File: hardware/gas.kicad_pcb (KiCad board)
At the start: 2 copper layers, 50 x 30 mm, 41 parts, among them P1 CON-SENSOR2, P10 3, P2 DEBUG, P3 BOOT, P7 0, P8 1, P9 2, U1 XMC1300, U10 MCP3423, U11 spec-sensor, U2 DRILL, U3 DRILL, U4 DRILL, U5 DRILL, U6 HDC1080, U7 ISL60002, U8 LMP91000, U9 MCP6041

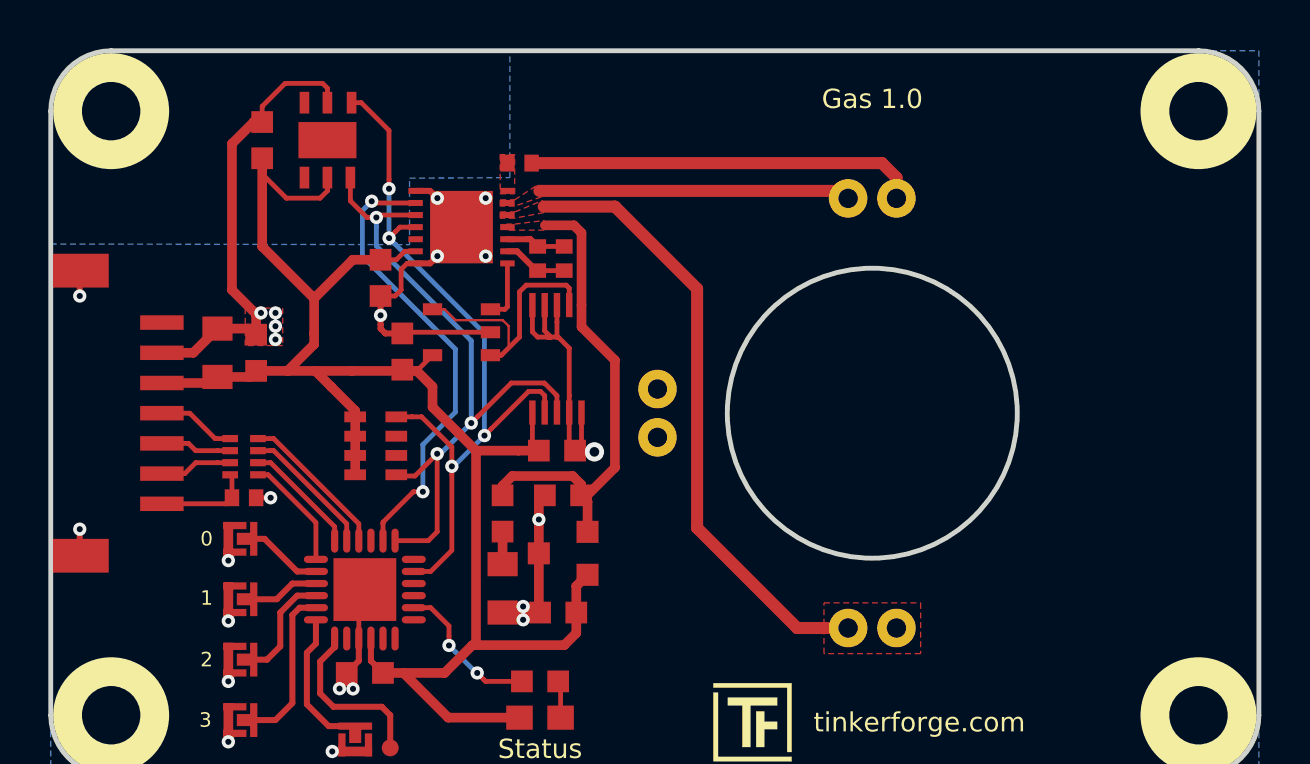
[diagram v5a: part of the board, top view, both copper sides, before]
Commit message: add fiducials
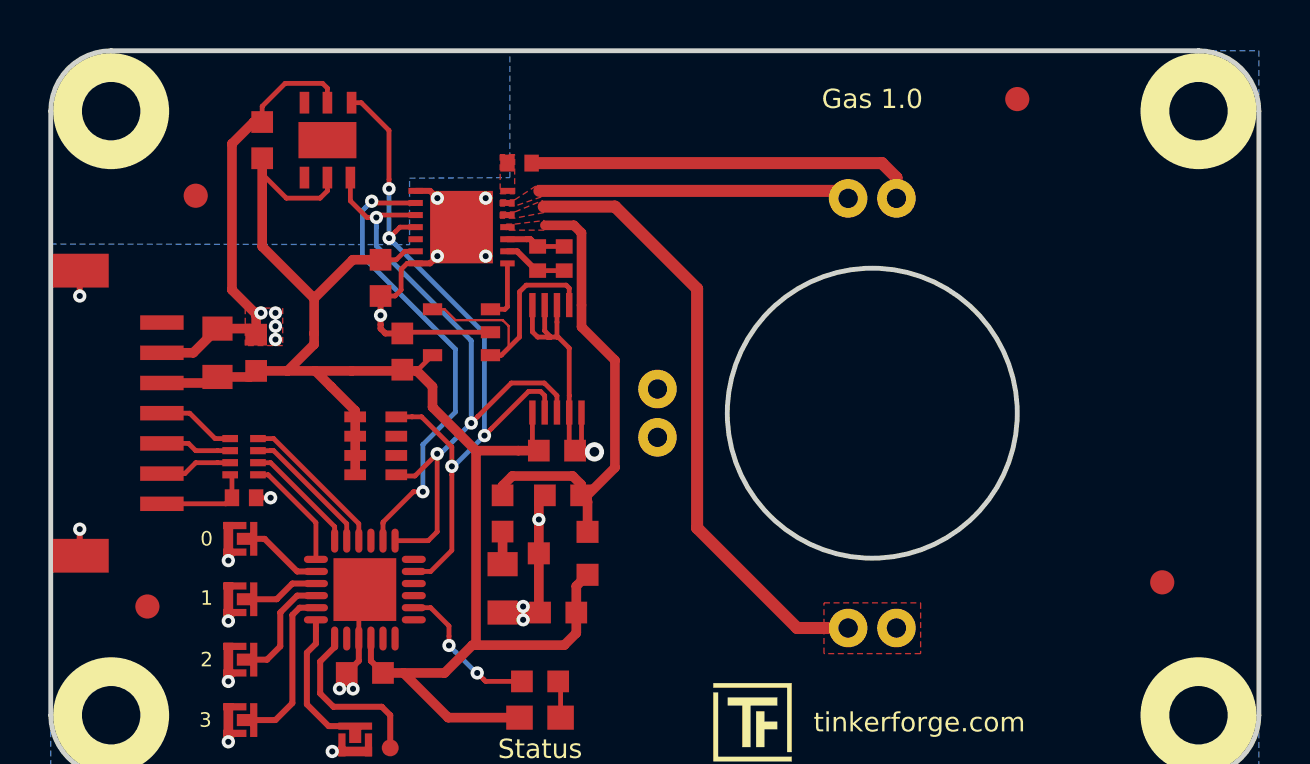
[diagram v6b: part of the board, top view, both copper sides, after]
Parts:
- added Fiducial_Mark: VAL**, kicad-libraries:Fiducial_Mark, F.Cu at (131.0, 122.1)
- added Fiducial_Mark: VAL**, kicad-libraries:Fiducial_Mark, F.Cu at (129.0, 139.1)
- added Fiducial_Mark: VAL**, kicad-libraries:Fiducial_Mark, F.Cu at (171.0, 138.1)
- added Fiducial_Mark: VAL**, kicad-libraries:Fiducial_Mark, F.Cu at (165.0, 118.1)
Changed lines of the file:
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@@
-(kicad_pcb (version 20171130) (host pcbnew 5.0.2-bee76a0~70~ubuntu18.10.1)
+(kicad_pcb (version 20171130) (host pcbnew 5.0.2-bee76a0~70~ubuntu18.04.1)
   (general
     (thickness 1.6)
@@
     (tracks 395)
     (zones 0)
-    (modules 41)
+    (modules 45)
     (nets 46)
   )
@@
   )
   (setup
-    (last_trace_width 0.4)
+    (last_trace_width 0.25)
     (user_trace_width 0.1)
     (user_trace_width 0.2)
@@
       (xy -1.232151 -1.7863) (xy -1.155444 -1.784232) (xy -1.083326 -1.807455)) (layer B.SilkS) (width 0.01))
   )
+  (module kicad-libraries:Fiducial_Mark (layer F.Cu)
+    (at 131 122.11)
+    (attr smd)
+    (fp_text reference Fiducial_Mark (at 0 0) (layer F.SilkS) hide
+      (effects (font (size 0.127 0.127) (thickness 0.03302)))
+    )
+    (fp_text value VAL** (at 0 -0.29972) (layer F.SilkS) hide
+      (effects (font (size 0.127 0.127) (thickness 0.03302)))
+    )
+    (fp_circle (center 0 0) (end 1.15062 0) (layer Dwgs.User) (width 0.01016))
+    (pad 1 smd circle (at 0 0) (size 1.00076 1.00076) (layers F.Cu F.Paste F.Mask)
+      (clearance 0.65024))
+  )
+  (module kicad-libraries:Fiducial_Mark (layer F.Cu)
+    (at 129 139.11)
+    (attr smd)
+    (fp_text reference Fiducial_Mark (at 0 0) (layer F.SilkS) hide
+      (effects (font (size 0.127 0.127) (thickness 0.03302)))
+    )
+    (fp_text value VAL** (at 0 -0.29972) (layer F.SilkS) hide
+      (effects (font (size 0.127 0.127) (thickness 0.03302)))
+    )
+    (fp_circle (center 0 0) (end 1.15062 0) (layer Dwgs.User) (width 0.01016))
+    (pad 1 smd circle (at 0 0) (size 1.00076 1.00076) (layers F.Cu F.Paste F.Mask)
+      (clearance 0.65024))
+  )
+  (module kicad-libraries:Fiducial_Mark (layer F.Cu)
+    (at 171 138.11)
+    (attr smd)
+    (fp_text reference Fiducial_Mark (at 0 0) (layer F.SilkS) hide
+      (effects (font (size 0.127 0.127) (thickness 0.03302)))
+    )
+    (fp_text value VAL** (at 0 -0.29972) (layer F.SilkS) hide
+      (effects (font (size 0.127 0.127) (thickness 0.03302)))
+    )
+    (fp_circle (center 0 0) (end 1.15062 0) (layer Dwgs.User) (width 0.01016))
+    (pad 1 smd circle (at 0 0) (size 1.00076 1.00076) (layers F.Cu F.Paste F.Mask)
+      (clearance 0.65024))
+  )
+  (module kicad-libraries:Fiducial_Mark (layer F.Cu)
+    (at 165 118.11)
+    (attr smd)
+    (fp_text reference Fiducial_Mark (at 0 0) (layer F.SilkS) hide
+      (effects (font (size 0.127 0.127) (thickness 0.03302)))
+    )
+    (fp_text value VAL** (at 0 -0.29972) (layer F.SilkS) hide
+      (effects (font (size 0.127 0.127) (thickness 0.03302)))
+    )
+    (fp_circle (center 0 0) (end 1.15062 0) (layer Dwgs.User) (width 0.01016))
+    (pad 1 smd circle (at 0 0) (size 1.00076 1.00076) (layers F.Cu F.Paste F.Mask)
+      (clearance 0.65024))
+  )
   (gr_text tinkerforge.com (at 160.95 143.91) (layer F.SilkS)
